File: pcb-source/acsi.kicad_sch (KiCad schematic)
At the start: 23 parts, among them J10 ST ACSI BUS, Q3 BC847, Q4 BC847, U1 74LVC245, U11 74LVC8T245

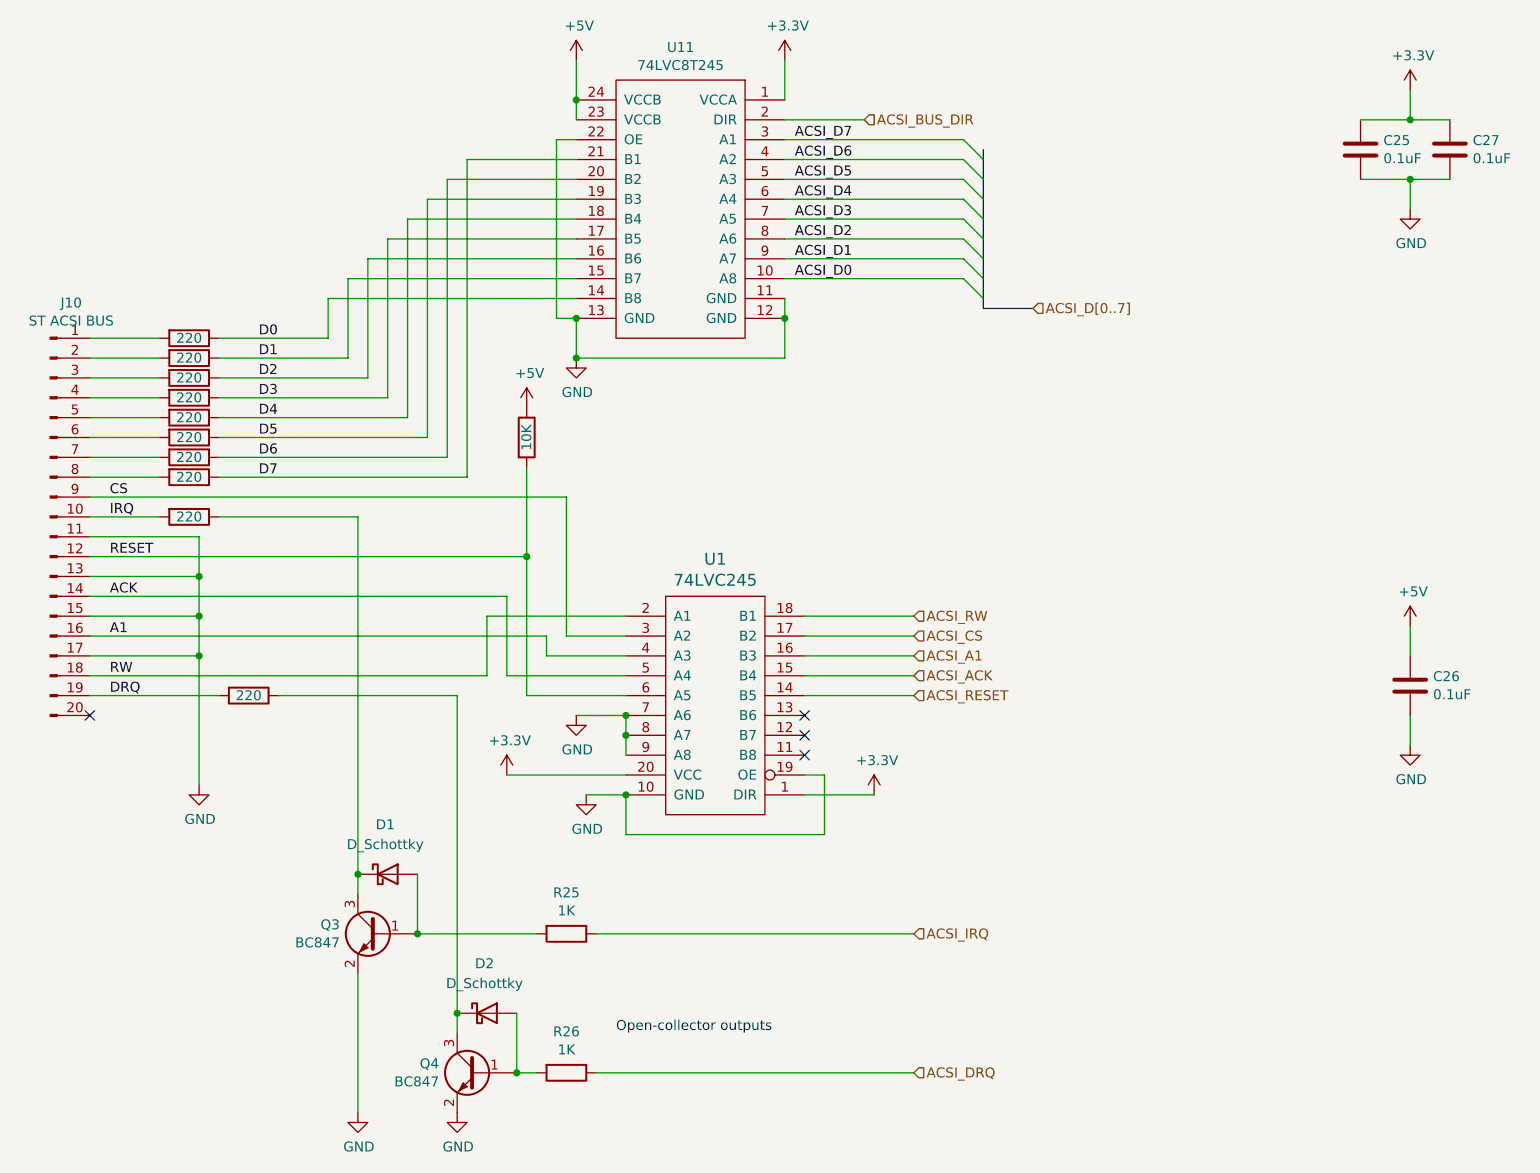
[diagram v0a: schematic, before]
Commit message: 1.2 version with 2 SPI buses
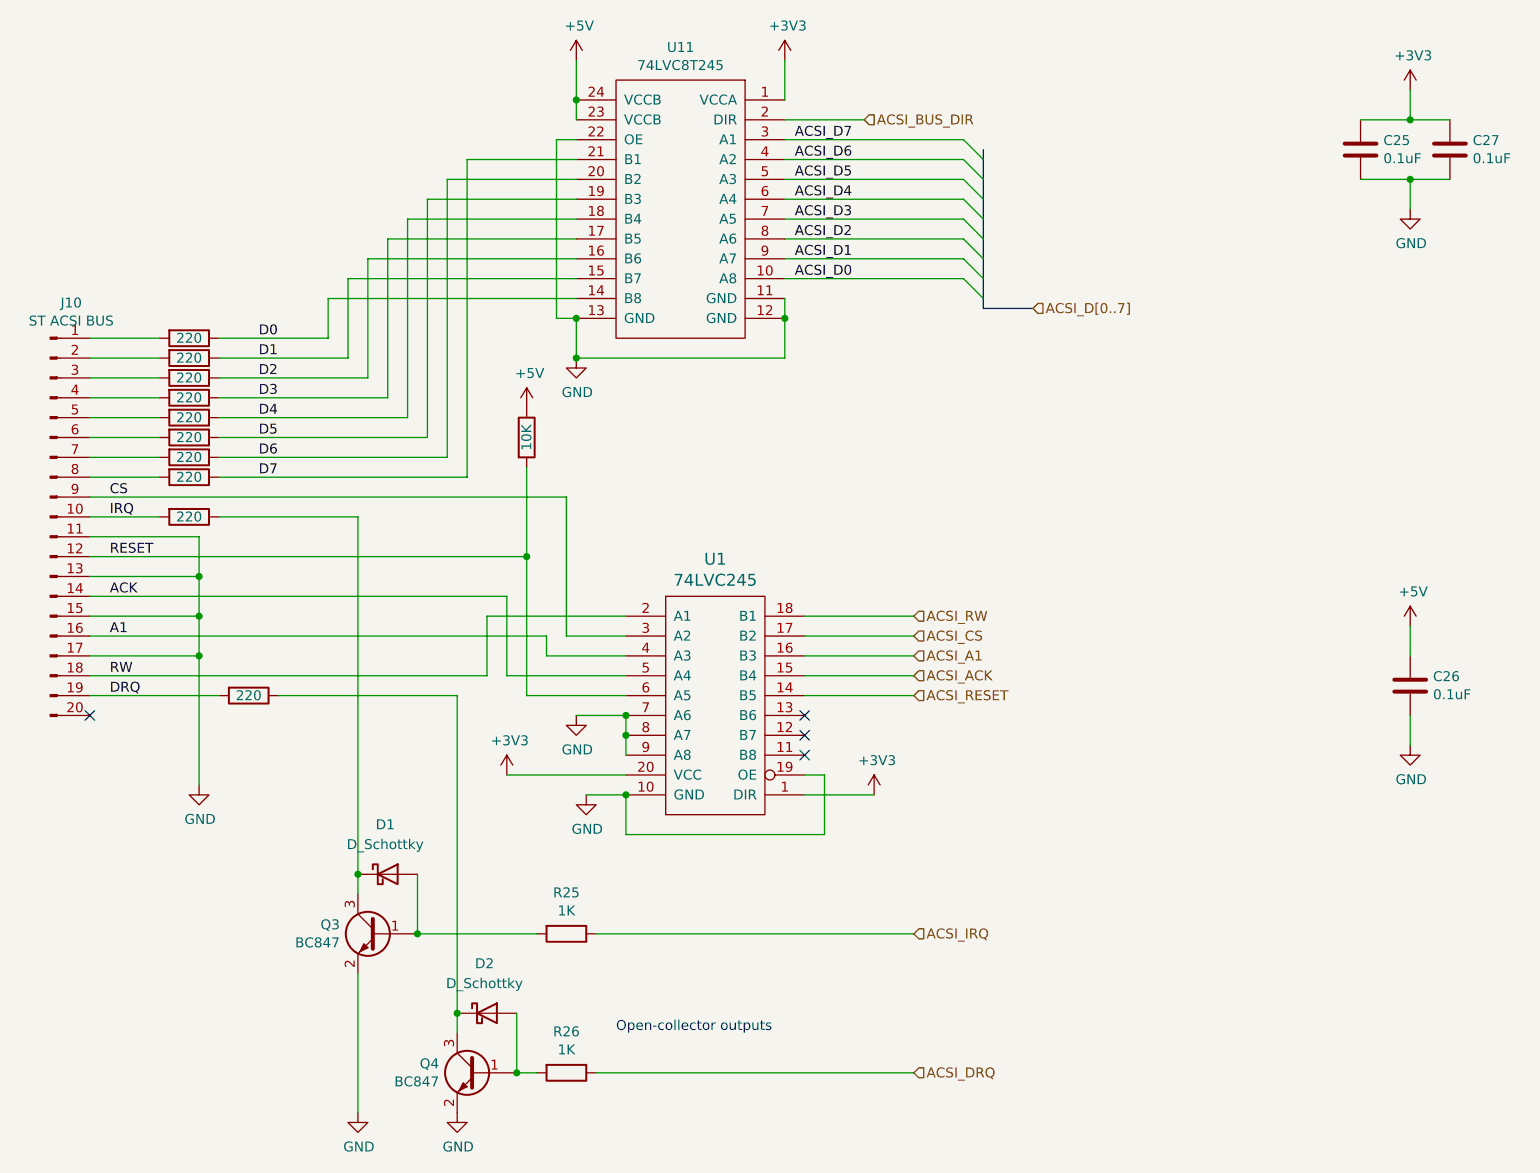
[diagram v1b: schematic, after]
